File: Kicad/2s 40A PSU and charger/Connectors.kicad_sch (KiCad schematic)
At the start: 5 parts

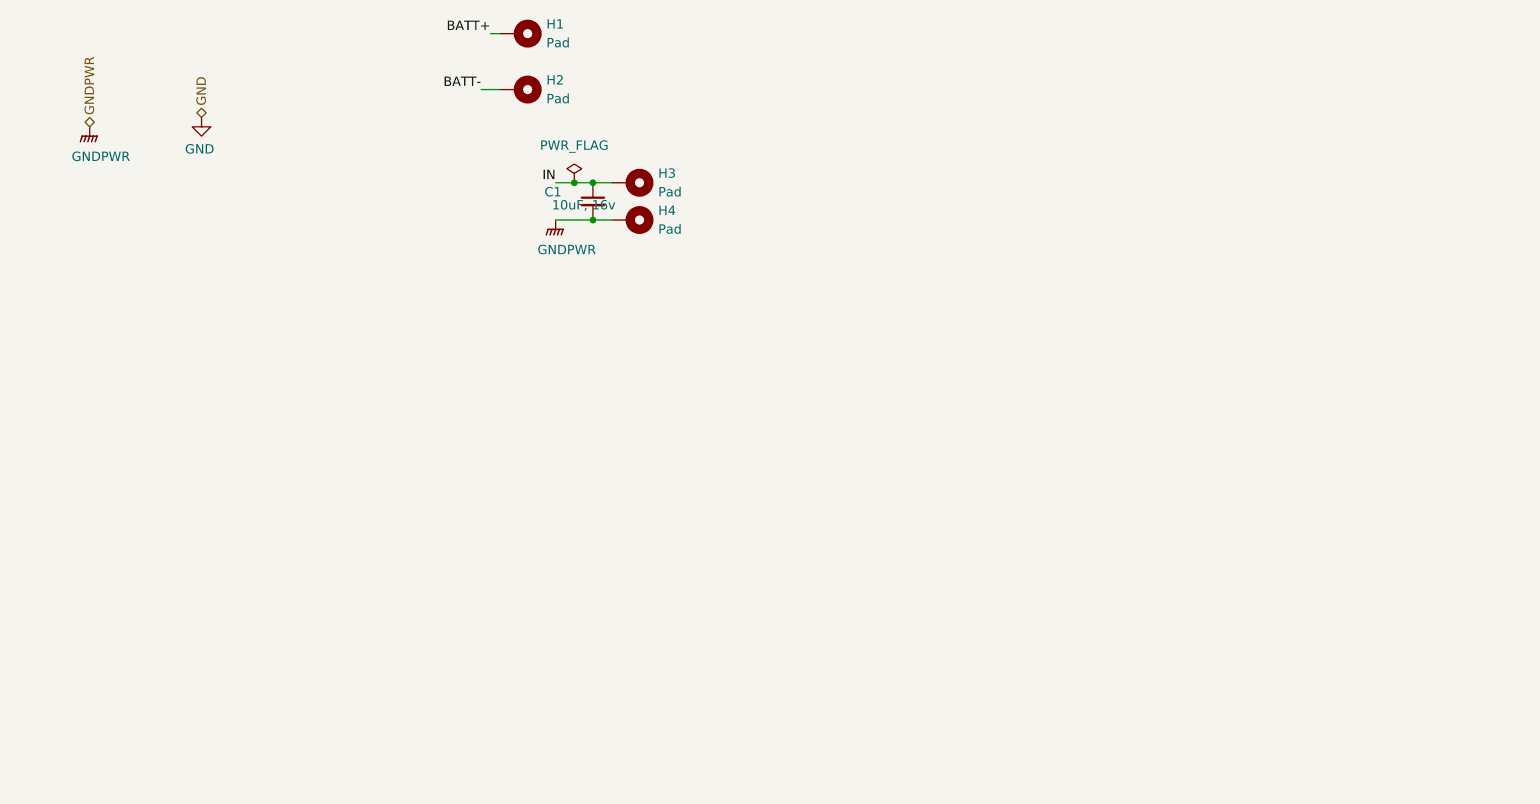
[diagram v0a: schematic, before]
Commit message: Reworked PSU to use CH32X035 and USB-PD
This will save a few bucks and will actually be a cooler solution than just a DC jack connected to some pads
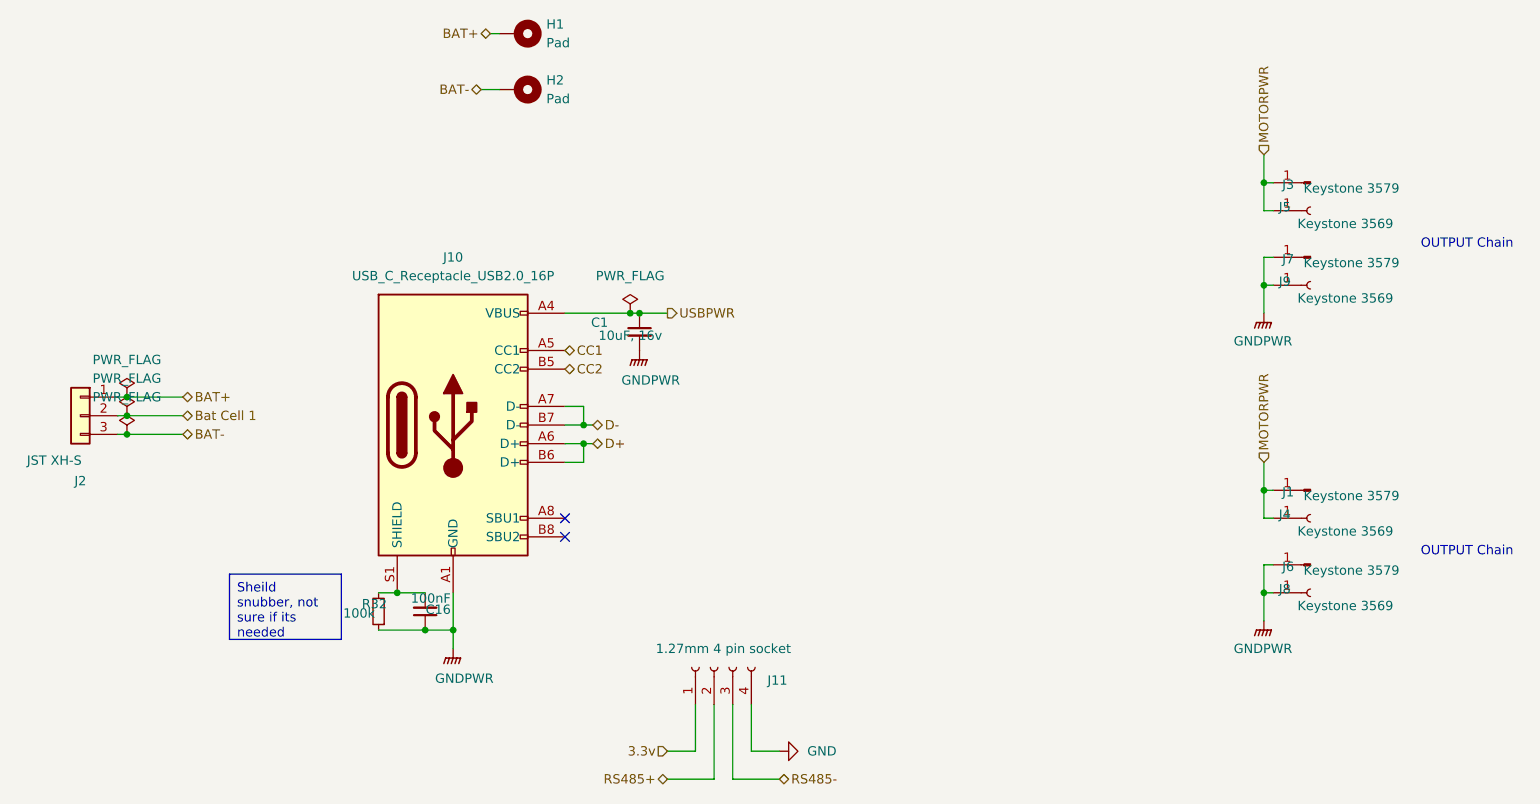
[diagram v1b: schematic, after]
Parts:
- removed H3, H4: Pad, TestPoint:TestPoint_Pad_3.0x3.0mm, symbol Mechanical:MountingHole_Pad
- added C16: 100nF, Capacitor_SMD:C_0402_1005Metric, symbol Device:C_Small
- added J1, J3, J6, J7: Keystone 3579, custom_Connector:Keystone_3579, symbol Connector:Conn_01x01_Pin
- added J10: USB_C_Receptacle_USB2.0_16P, Connector_USB:USB_C_Receptacle_XKB_U262-16XN-4BVC11, symbol Connector:USB_C_Receptacle_USB2.0_16P
- added J11: 1.27mm 4 pin socket, Connector_PinSocket_1.27mm:PinSocket_1x04_P1.27mm_Vertical, symbol Connector:Conn_01x04_Socket
- added J2: JST XH-S, Connector_JST:JST_XH_S3B-XH-A_1x03_P2.50mm_Horizontal, symbol Connector_Generic:Conn_01x03
- added J4, J5, J8, J9: Keystone 3569, custom_Connector:Keystone_3569, symbol Connector:Conn_01x01_Socket
- added R32: 100k, Resistor_SMD:R_0402_1005Metric, symbol Device:R_Small
- C1: footprint Capacitor_SMD:C_0603_1608Metric_Pad1.08x0.95mm_HandSolder -> Capacitor_SMD:C_0805_2012Metric
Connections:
- net GND: now also J11.4 (Pin_4)
- net GNDPWR: now also C16.1, J10.A1 (GND), J10.A12 (GND), J10.B1 (GND), J10.B12 (GND), J6.1 (Pin_1), J7.1 (Pin_1), J8.1 (Pin_1), J9.1 (Pin_1), R32.1
- net BATT+ renamed BAT+
- net BAT+: now also J2.1 (Pin_1)
- net BATT- renamed BAT-
- net BAT-: now also J2.3 (Pin_3)
- net IN renamed USBPWR
- net USBPWR: now also J10.A4 (VBUS), J10.A9 (VBUS), J10.B4 (VBUS), J10.B9 (VBUS)
- new net: C16.2, J10.S1 (SHIELD), R32.2
- new net 3.3v: J11.1 (Pin_1)
- new net Bat Cell 1: J2.2 (Pin_2)
- new net CC1: J10.A5 (CC1)
- new net CC2: J10.B5 (CC2)
- new net D+: J10.A6 (D+), J10.B6 (D+)
- new net D-: J10.A7 (D-), J10.B7 (D-)
- new net MOTORPWR: J1.1 (Pin_1), J3.1 (Pin_1), J4.1 (Pin_1), J5.1 (Pin_1)
- new net RS485+: J11.2 (Pin_2)
- new net RS485-: J11.3 (Pin_3)
- no-connect marks 0 -> 2
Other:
- note added: "OUTPUT Chain"
- moved on the sheet: C1

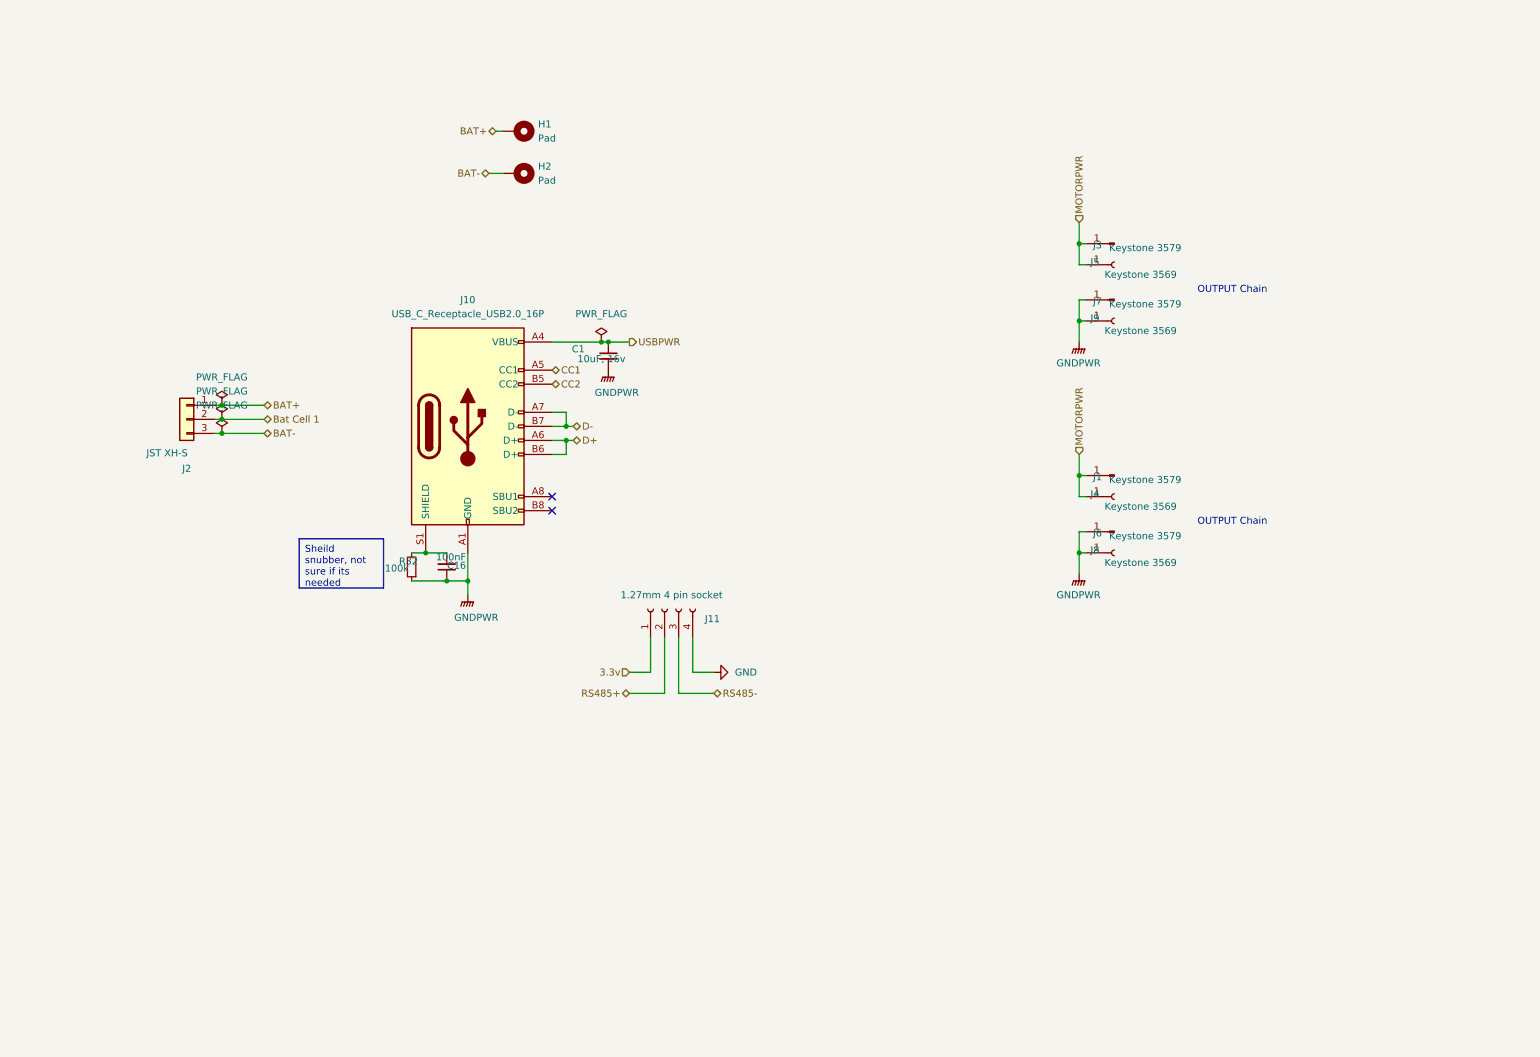
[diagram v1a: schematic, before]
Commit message: Improved schematic formatting and visuals
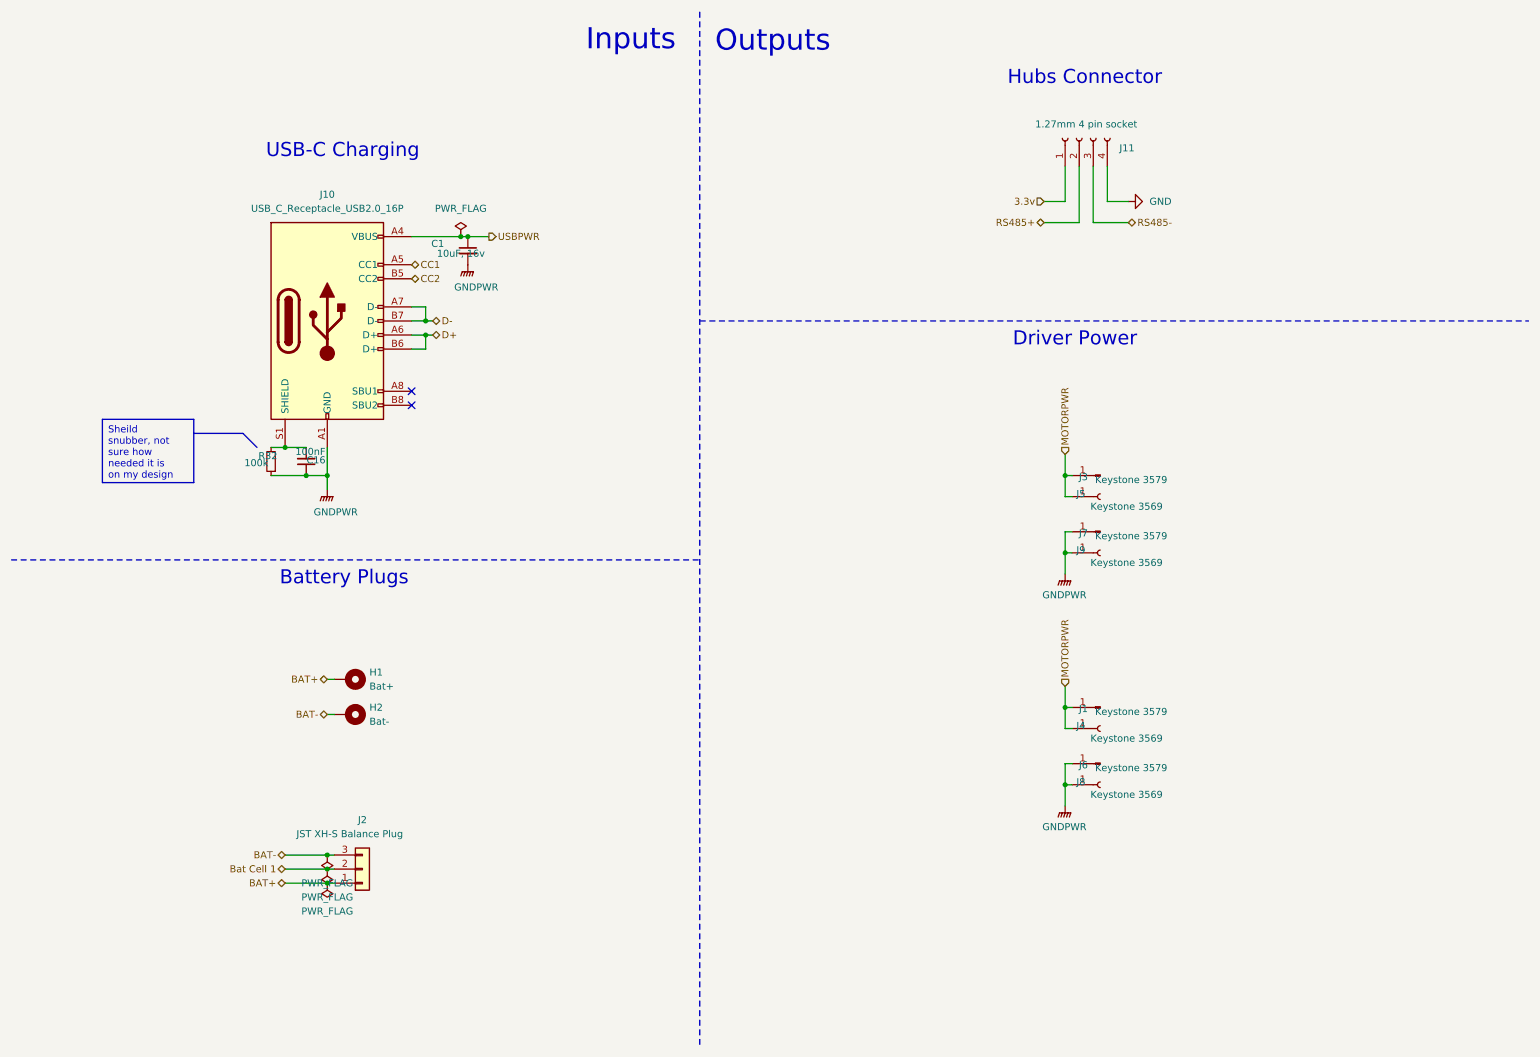
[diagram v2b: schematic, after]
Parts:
- H1: value Pad -> Bat+
- H2: value Pad -> Bat-
- J2: value JST XH-S -> JST XH-S Balance Plug
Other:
- note added: "Battery Plugs"
- note added: "Driver Power"
- note added: "Hubs Connector"
- note added: "Inputs"
- note added: "Outputs"
- note added: "USB-C Charging"
- note removed: "OUTPUT Chain"
- moved on the sheet: C1, C16, H1, H2, J1, J10, J11, J2, J3, J4, J5, J6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

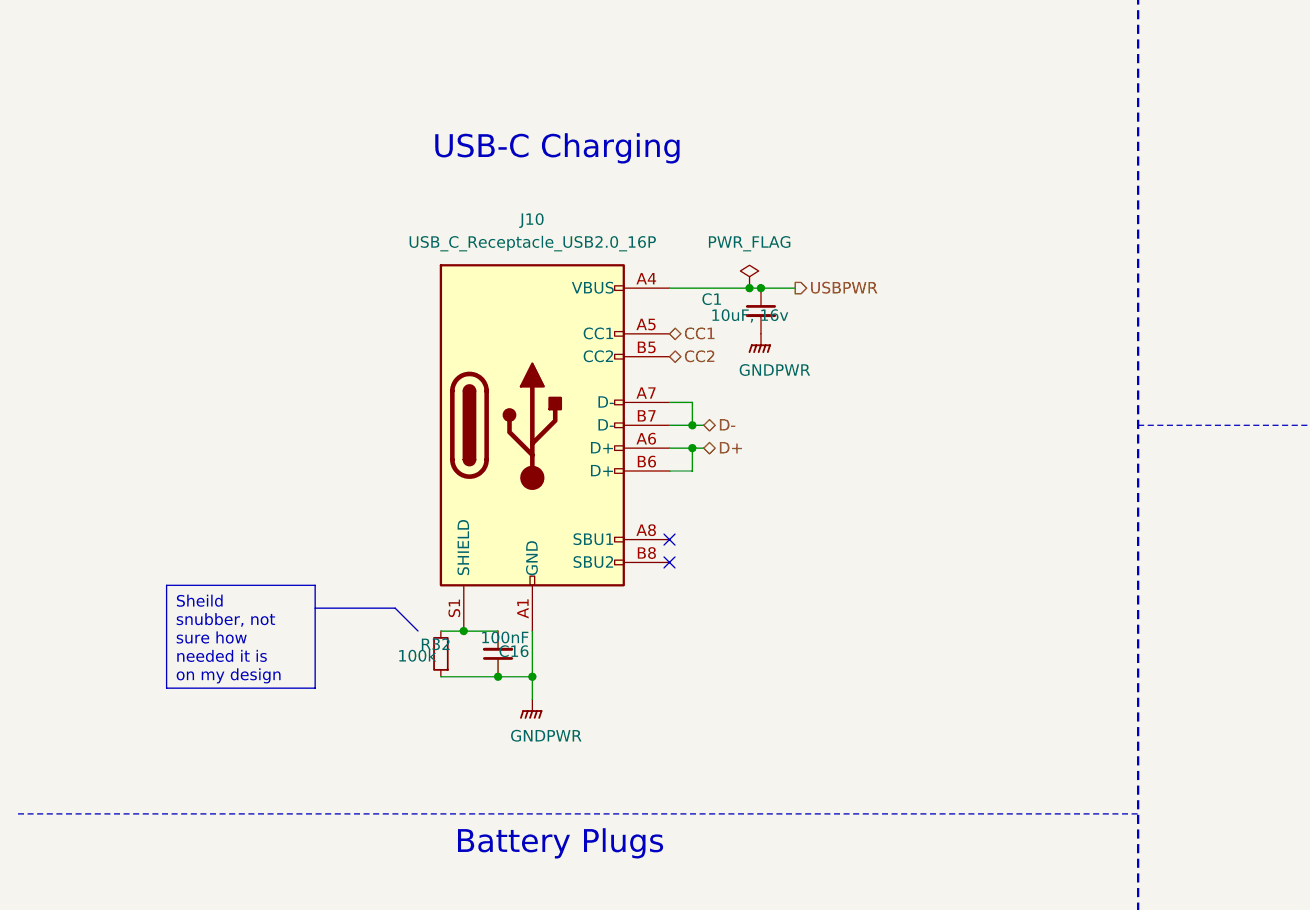
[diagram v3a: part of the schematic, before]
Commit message: Add proper ESD protection and pulldowns for USB-C
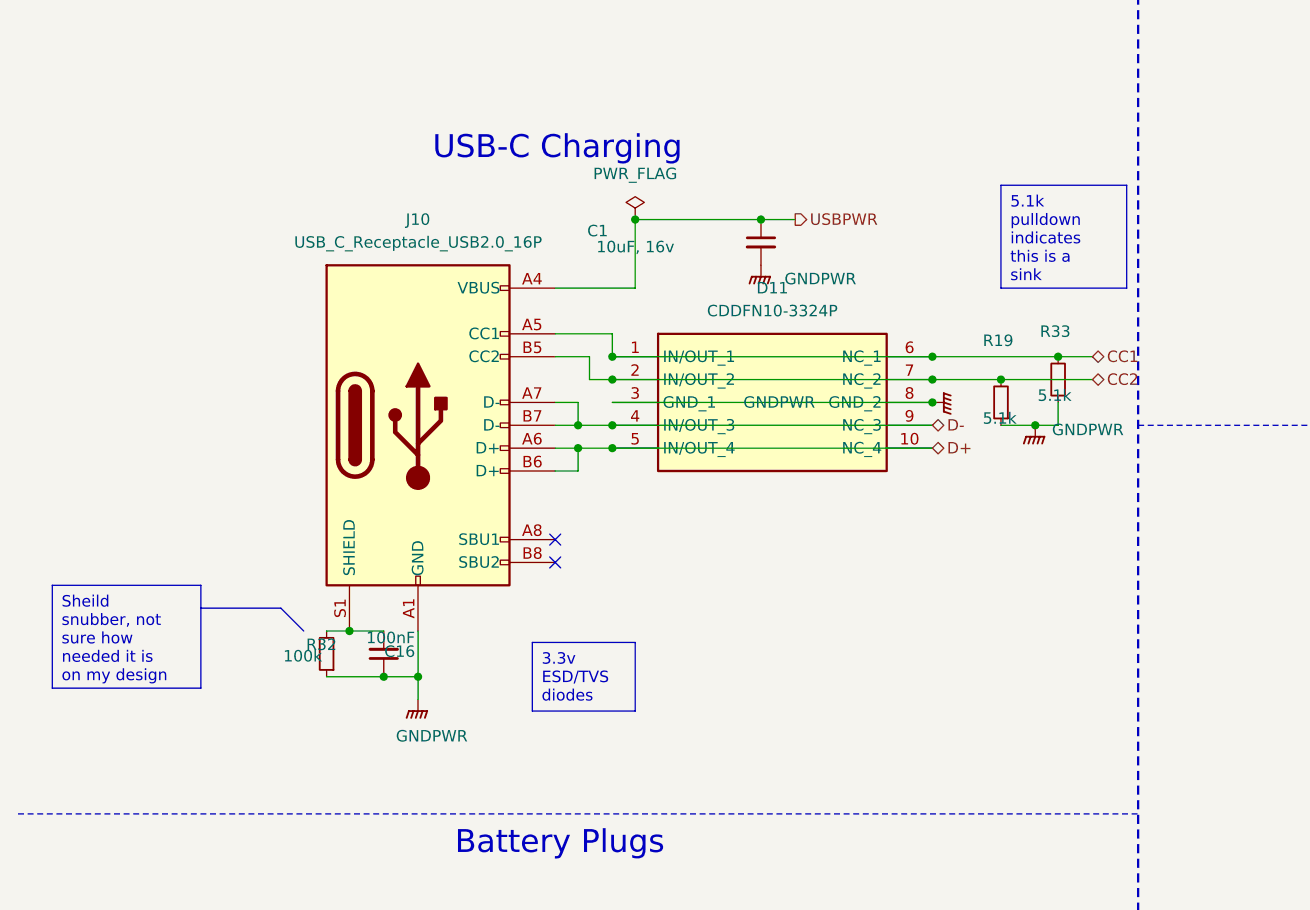
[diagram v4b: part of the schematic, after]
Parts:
- added D11: CDDFN10-3324P, CDDFN10-3324P:CDDFN103324P, symbol CDDFN10-3324P:CDDFN10-3324P
- added R19, R33: 5.1k, Resistor_SMD:R_0402_1005Metric, symbol Device:R_Small
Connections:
- net CC1: now also D11.1 (IN/OUT_1), D11.6 (NC_1), R33.2
- net CC2: now also D11.2 (IN/OUT_2), D11.7 (NC_2), R19.2
- net D+: now also D11.10 (NC_4), D11.5 (IN/OUT_4)
- net D-: now also D11.4 (IN/OUT_3), D11.9 (NC_3)
- net GNDPWR: now also D11.3 (GND_1), D11.8 (GND_2), R19.1, R33.1
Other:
- moved on the sheet: C1, C16, J10, R32
